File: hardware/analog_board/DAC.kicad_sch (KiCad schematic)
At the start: 112 parts, among them Q1 MMBT3906, Q2 MMBT3906, U3 AD9747BCPZ, U4 OPA695ID, U5 OPA695ID, U6 NE5532

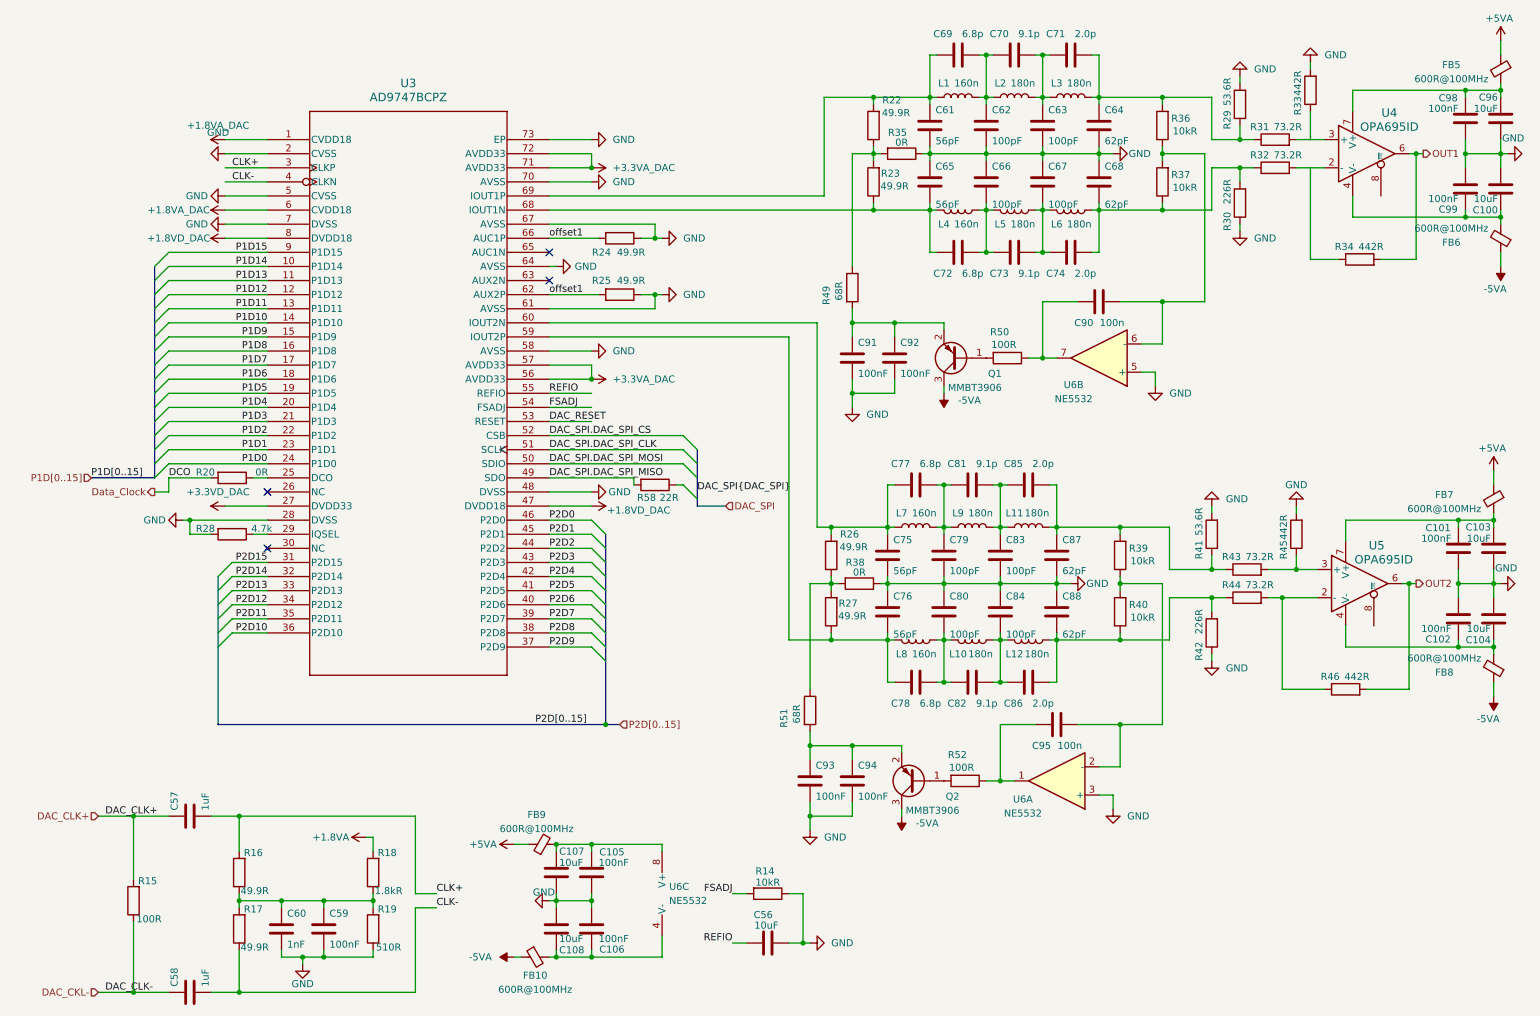
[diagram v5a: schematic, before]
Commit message: feat：原理图添加测试点
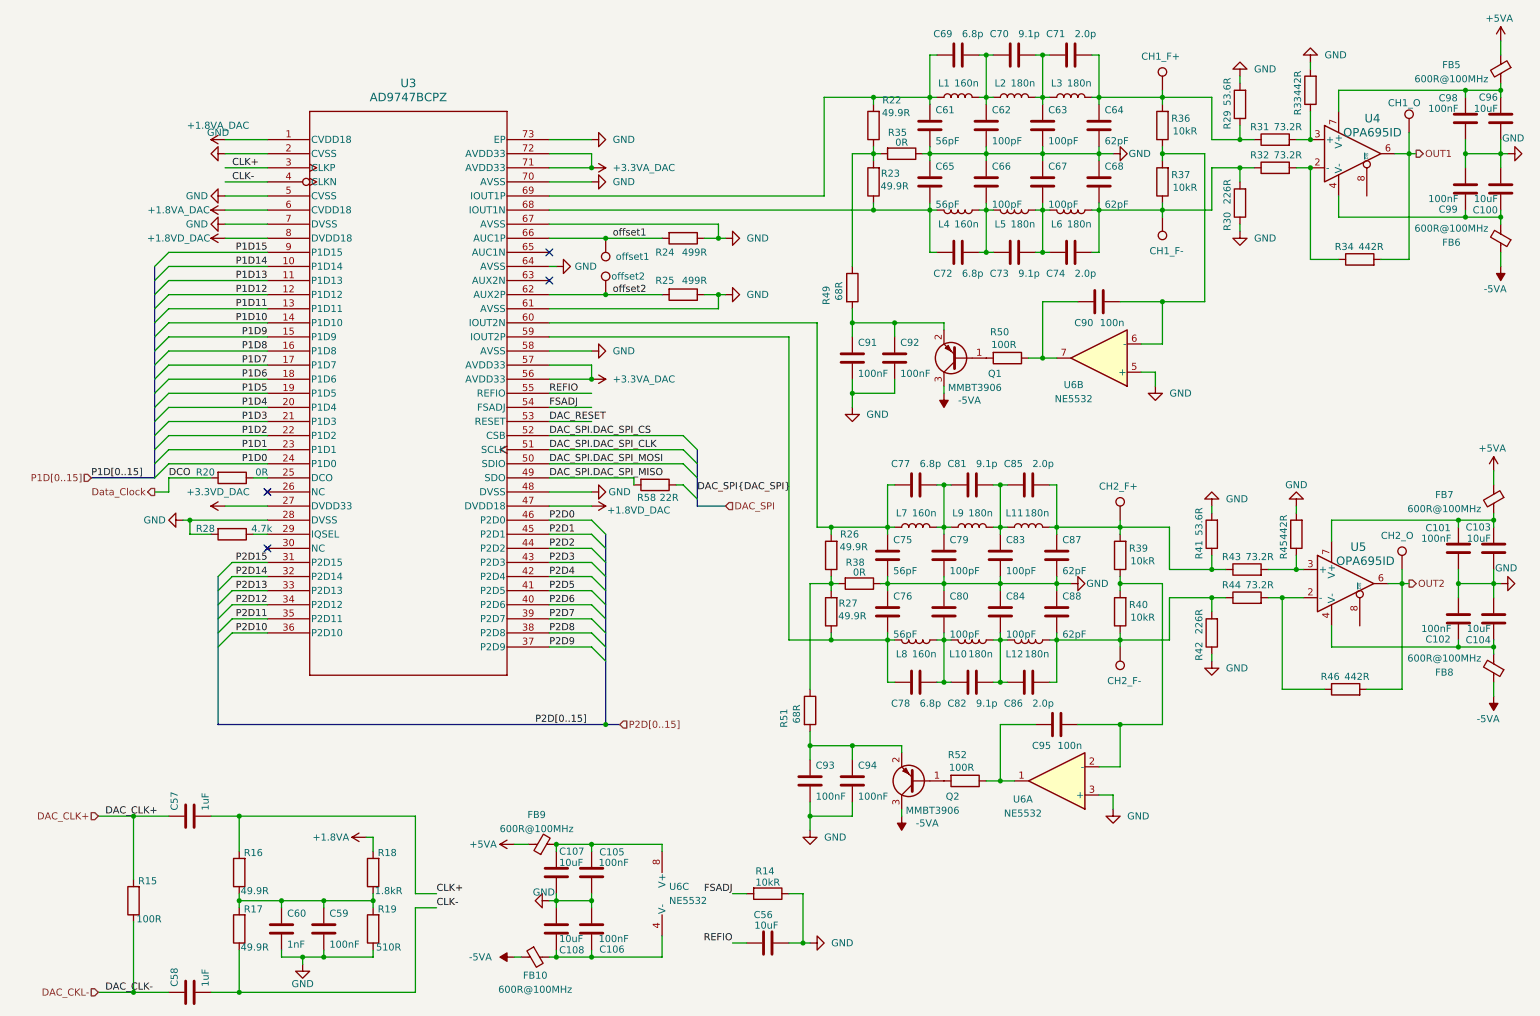
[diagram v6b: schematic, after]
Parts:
- added TP1: CH1_O, TestPoint:TestPoint_Pad_D1.0mm, symbol Connector:TestPoint
- added TP2: CH2_O, TestPoint:TestPoint_Pad_D1.0mm, symbol Connector:TestPoint
- added TP3: CH2_F+, TestPoint:TestPoint_Pad_D1.0mm, symbol Connector:TestPoint
- added TP4: CH2_F-, TestPoint:TestPoint_Pad_D1.0mm, symbol Connector:TestPoint
- added TP5: CH1_F+, TestPoint:TestPoint_Pad_D1.0mm, symbol Connector:TestPoint
- added TP6: CH1_F-, TestPoint:TestPoint_Pad_D1.0mm, symbol Connector:TestPoint
- added TP7: offset1, TestPoint:TestPoint_Pad_D1.0mm, symbol Connector:TestPoint
- added TP8: offset2, TestPoint:TestPoint_Pad_D1.0mm, symbol Connector:TestPoint
- R24, R25: value 49.9R -> 499R
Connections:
- net OUT1: now also TP1.1
- net OUT2: now also TP2.1
- net offset1: now also TP7.1; no longer R25.2, U3.62 (AUX2P)
- net at C85.1, C87.2, L11.2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: now also TP3.1
- net at C86.1, C88.1, L12.2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: now also TP4.1
- net at C64.2, C71.1, L3.2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: now also TP5.1
- net at C68.1, C74.1, L6.2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: now also TP6.1
- new net offset2: R25.2, TP8.1, U3.62 (AUX2P)
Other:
- moved on the sheet: R24, R25, U4, U5

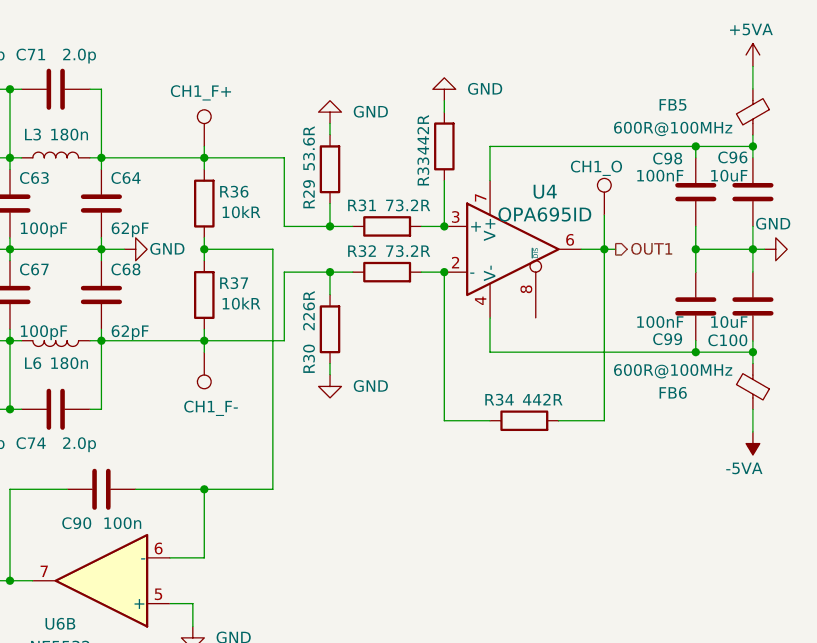
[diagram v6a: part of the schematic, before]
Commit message: feat：差分转单端预布局
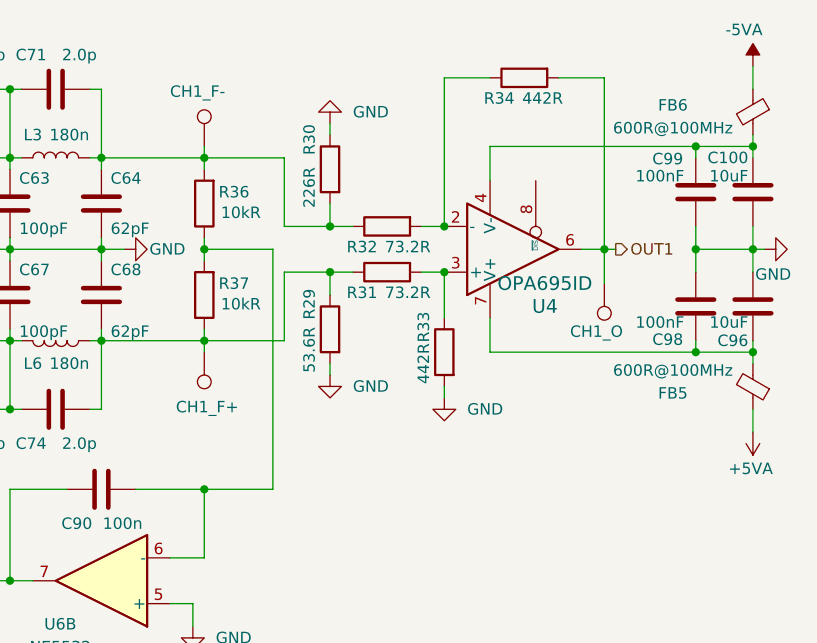
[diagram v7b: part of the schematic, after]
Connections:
- net at C64.2, C71.1, L3.2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: now also R30.2, R32.1, TP6.1; no longer R29.1, R31.1, TP5.1
- net at C68.1, C74.1, L6.2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: now also R29.1, R31.1, TP5.1; no longer R30.2, R32.1, TP6.1

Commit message: feat：时钟电路预布局
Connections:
- net DAC_CKL- renamed DAC_CLK-
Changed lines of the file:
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@@
-		)
-	)
-	(label "DAC_CLK-"
-		(at 27.94 193.04 0)
-		(effects
-			(font
-				(size 1.27 1.27)
-			)
-			(justify left bottom)
-		)
-	)
-	(label "DAC_CLK+"
-		(at 27.94 161.29 0)
-		(effects
-			(font
-				(size 1.27 1.27)
-			)
-			(justify left bottom)
 		)
 	)
@@
 		)
 	)
-	(hierarchical_label "DAC_CKL-"
+	(hierarchical_label "DAC_CLK-"
 		(shape input)
 		(at 26.67 193.04 180)
